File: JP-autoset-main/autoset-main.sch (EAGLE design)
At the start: 120 parts, among them J1 TERM_1X2_0.1, J10 TERM_1X2_0.1, J11 TERM_1X2_0.1, J12 TERM_1X2_0.1, J2 TERM_1X6_0.1, J3 TERM_1X2_0.1, J4 TERM_1X4_0.1, J5 TERM_1X2_0.1, J6 TERM_1X2_0.1, J7 TERM_1X2_0.1, J8 TERM_1X2_0.1, J9 TERM_1X2_0.1, P1 RECT_1X8, P2 RECT_1X6, P3 RECT_1X8, P4 RECT_1X10, Q1 NMOS-RUC002N05, Q2 NMOS-RUC002N05, Q3 NMOS-RUC002N05, Q4 NMOS-RUC002N05, Q5 NMOS-RUC002N05, Q7 PMOS-FQD7P06TM, U1 LM293DT, U10 QRE1113GR, U2 LM293DT, U3 QRE1113GR, U4 QRE1113GR, U5 QRE1113GR, U6 LD1085CDT-R, U8 A3909

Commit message: Multiple updates
Library update (add switch)
Updated sensing board to 4 layers, added some filtering.
Updated control board to 4 layers, added functionality.
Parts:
- removed D3, D4, D5, D6: LED, dsantoro-discrete:LED
- removed Z17: NC, dsantoro-dir:NC
- added R56: 0, dsantoro-discrete:R0603
- added SW1: GPTS203211B, dsantoro-sw:GPTS203211B
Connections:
- net BUTTON1: now also P3.2; no longer P3.3
- net BUTTON2: now also P3.3; no longer P3.2
- net LED1: now also P4.9; no longer P3.4
- net LED2: now also P4.8; no longer P4.7
- net LED3: now also P3.4; no longer P4.9
- net LED4: now also P4.7; no longer P4.8
- net N$12: no longer D3.C
- net N$14: no longer D3.A
- net N$16: no longer D4.A
- net N$18: no longer D5.C
- net N$19: no longer D5.A
- net N$20: no longer D6.C
- net N$23: no longer D6.A
- net N$4: no longer D4.C
- net N$5: now also R56.1, R7.2, R8.2, SW1.1; no longer P2.6, Z17.P$1
- net VCC: no longer C15.1, C16.1, C19.1, C23.1, R38.2, R39.2, R45.2, R50.2, R52.2, R53.2, R54.2, R55.2
- net VCOPT1: now also P2.1; no longer P2.4
- net VCOPT2: now also P2.2; no longer P2.3
- net VCOPT3: now also P2.3; no longer P2.2
- net VCOPT4: now also P2.4; no longer P2.1
- net VDD: now also C15.1, C16.1, C19.1, C23.1, R38.2, R39.2, R45.2, R50.2, R52.2, R53.2, R54.2, R55.2, R56.2, SW1.2; no longer R7.2, R8.2
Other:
- moved on the sheet: P1, P4, R32, R33, R7, R8

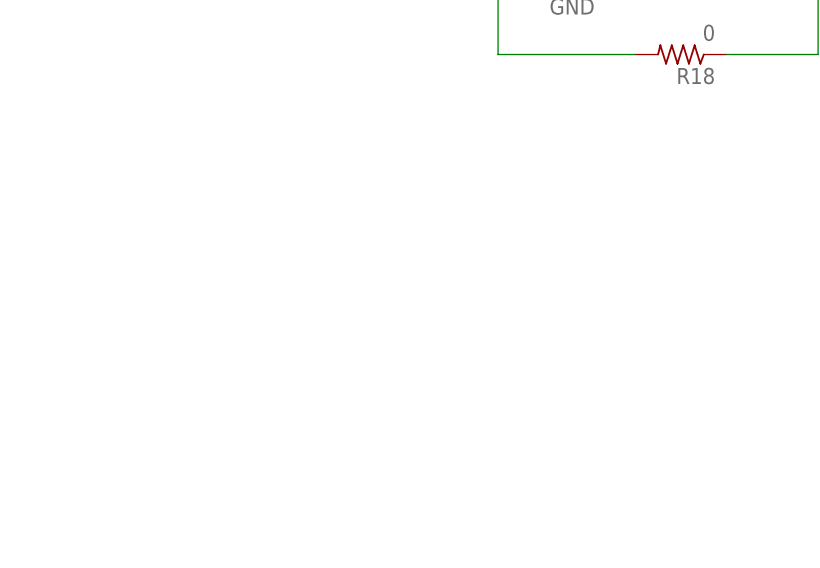
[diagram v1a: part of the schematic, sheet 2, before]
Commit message: Updates
Sensing manufacture. Updated library. Updated main schematic to include
magnetic sensor.
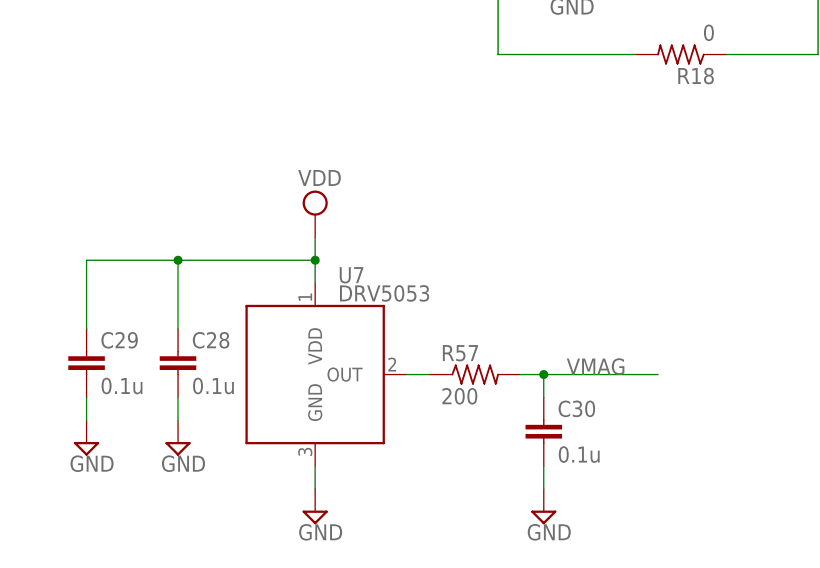
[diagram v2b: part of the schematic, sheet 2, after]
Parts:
- added C28, C29, C30: 0.1u, dsantoro-discrete:C0603
- added R57: 200, dsantoro-discrete:R0603
- added U7: DRV5053, dsantoro-sens:DRV5053
- SW1: DKPN (none) -> CW181-ND
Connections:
- new net N$25: R57.1, U7.OUT
- new net VMAG: C30.1, P2.6, R57.2
- net GND: now also C28.2, C29.2, C30.2, U7.GND
- net VDD: now also C28.1, C29.1, U7.VDD
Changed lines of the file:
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@@
 <setting verticaltext="up"/>
 </settings>
-<grid distance="0.1" unitdist="inch" unit="inch" style="lines" multiple="1" display="no" altdistance="0.025" altunitdist="inch" altunit="inch"/>
+<grid distance="0.1" unitdist="inch" unit="inch" style="lines" multiple="1" display="no" altdistance="0.01" altunitdist="inch" altunit="inch"/>
 <layers>
 <layer number="1" name="Top" color="4" fill="1" visible="no" active="no"/>
@@
 <part name="SUPPLY83" library="supply2" deviceset="VDD" device=""/>
 <part name="SUPPLY97" library="supply2" deviceset="VDD" device=""/>
-<part name="SW1" library="dsantoro-sw" deviceset="GPTS203211B" device=""/>
+<part name="SW1" library="dsantoro-sw" deviceset="GPTS203211B" device="">
+<attribute name="DKPN" value="CW181-ND"/>
+</part>
 <part name="R56" library="dsantoro-discrete" deviceset="R" device="0603" value="0">
 <attribute name="DKPN" value="541-2779-1-ND"/>
 </part>
+<part name="U7" library="dsantoro-sens" deviceset="DRV5053" device=""/>
+<part name="C28" library="dsantoro-discrete" deviceset="C" device="0603" value="0.1u">
+<attribute name="DKPN" value="490-1519-1-ND"/>
+</part>
+<part name="C29" library="dsantoro-discrete" deviceset="C" device="0603" value="0.1u">
+<attribute name="DKPN" value="490-1519-1-ND"/>
+</part>
+<part name="SUPPLY42" library="supply2" deviceset="GND" device=""/>
+<part name="SUPPLY111" library="supply2" deviceset="GND" device=""/>
+<part name="SUPPLY112" library="supply2" deviceset="VDD" device=""/>
+<part name="SUPPLY113" library="supply2" deviceset="GND" device=""/>
+<part name="R57" library="dsantoro-discrete" deviceset="R" device="0603" value="200">
+<attribute name="DKPN" value="RHM200DCT-ND"/>
+</part>
+<part name="C30" library="dsantoro-discrete" deviceset="C" device="0603" value="0.1u">
+<attribute name="DKPN" value="490-1519-1-ND"/>
+</part>
+<part name="SUPPLY114" library="supply2" deviceset="GND" device=""/>
 </parts>
 <sheets>
@@
 <instance part="SUPPLY83" gate="G$1" x="312.42" y="157.48"/>
 <instance part="SUPPLY97" gate="G$1" x="358.14" y="157.48"/>
-<instance part="SW1" gate="G$1" x="22.86" y="220.98" rot="MR0"/>
+<instance part="SW1" gate="G$1" x="22.86" y="220.98" rot="MR0">
+<attribute name="DKPN" x="22.86" y="220.98" size="1.778" layer="96" rot="MR0" display="off"/>
+</instance>
 <instance part="R56" gate="G$1" x="24.13" y="228.6" rot="R180">
 <attribute name="DKPN" x="24.13" y="228.6" size="1.778" layer="96" rot="R180" display="off"/>
@@
 <wire x1="33.02" y1="228.6" x2="33.02" y2="220.98" width="0.1524" layer="91"/>
 <junction x="33.02" y="220.98"/>
+</segment>
+</net>
+<net name="VMAG" class="0">
+<segment>
+<pinref part="P2" gate="G$1" pin="6"/>
+<wire x1="22.86" y1="139.7" x2="35.56" y2="139.7" width="0.1524" layer="91"/>
+<label x="27.94" y="139.7" size="1.778" layer="95"/>
 </segment>
 </net>
@@
 <instance part="FRAME2" gate="G$1" x="0" y="0"/>
 <instance part="FRAME2" gate="G$2" x="180.34" y="7.62"/>
+<instance part="U7" gate="G$1" x="35.56" y="35.56"/>
+<instance part="C28" gate="G$1" x="27.94" y="30.48">
+<attribute name="DKPN" x="27.94" y="30.48" size="1.778" layer="96" display="off"/>
+</instance>
+<instance part="C29" gate="G$1" x="17.78" y="30.48">
+<attribute name="DKPN" x="17.78" y="30.48" size="1.778" layer="96" display="off"/>
+</instance>
+<instance part="SUPPLY42" gate="GND" x="17.78" y="20.32"/>
+<instance part="SUPPLY111" gate="GND" x="27.94" y="20.32"/>
+<instance part="SUPPLY112" gate="G$1" x="43.18" y="45.72"/>
+<instance part="SUPPLY113" gate="GND" x="43.18" y="12.7"/>
+<instance part="R57" gate="G$1" x="60.96" y="27.94">
+<attribute name="DKPN" x="60.96" y="27.94" size="1.778" layer="96" display="off"/>
+</instance>
+<instance part="C30" gate="G$1" x="68.58" y="22.86">
+<attribute name="DKPN" x="68.58" y="22.86" size="1.778" layer="96" display="off"/>
+</instance>
+<instance part="SUPPLY114" gate="GND" x="68.58" y="12.7"/>
 </instances>
 <busses>
@@
 <pinref part="U1" gate="A" pin="V-"/>
 <pinref part="SUPPLY5" gate="GND" pin="GND"/>
+</segment>
+<segment>
+<pinref part="C29" gate="G$1" pin="2"/>
+<pinref part="SUPPLY42" gate="GND" pin="GND"/>
+<wire x1="17.78" y1="22.86" x2="17.78" y2="25.4" width="0.1524" layer="91"/>
+</segment>
+<segment>
+<pinref part="C28" gate="G$1" pin="2"/>
+<pinref part="SUPPLY111" gate="GND" pin="GND"/>
+<wire x1="27.94" y1="22.86" x2="27.94" y2="25.4" width="0.1524" layer="91"/>
+</segment>
+<segment>
+<pinref part="U7" gate="G$1" pin="GND"/>
+<pinref part="SUPPLY113" gate="GND" pin="GND"/>
+<wire x1="43.18" y1="15.24" x2="43.18" y2="17.78" width="0.1524" layer="91"/>
+</segment>
+<segment>
+<pinref part="C30" gate="G$1" pin="2"/>
+<pinref part="SUPPLY114" gate="GND" pin="GND"/>
+<wire x1="68.58" y1="15.24" x2="68.58" y2="17.78" width="0.1524" layer="91"/>
 </segment>
 </net>
@@
 <pinref part="SUPPLY3" gate="G$1" pin="VDD"/>
 </segment>
+<segment>
+<pinref part="U7" gate="G$1" pin="VDD"/>
+<pinref part="SUPPLY112" gate="G$1" pin="VDD"/>
+<wire x1="43.18" y1="43.18" x2="43.18" y2="40.64" width="0.1524" layer="91"/>
+<pinref part="C28" gate="G$1" pin="1"/>
+<wire x1="43.18" y1="40.64" x2="43.18" y2="38.1" width="0.1524" layer="91"/>
+<wire x1="43.18" y1="40.64" x2="27.94" y2="40.64" width="0.1524" layer="91"/>
+<wire x1="27.94" y1="40.64" x2="27.94" y2="33.02" width="0.1524" layer="91"/>
+<junction x="43.18" y="40.64"/>
+<pinref part="C29" gate="G$1" pin="1"/>
+<wire x1="27.94" y1="40.64" x2="17.78" y2="40.64" width="0.1524" layer="91"/>
+<wire x1="17.78" y1="40.64" x2="17.78" y2="33.02" width="0.1524" layer="91"/>
+<junction x="27.94" y="40.64"/>
+</segment>
 </net>
 <net name="N$44" class="0">
@@
 </segment>
 </net>
+<net name="N$25" class="0">
+<segment>
+<pinref part="U7" gate="G$1" pin="OUT"/>
+<pinref part="R57" gate="G$1" pin="1"/>
+<wire x1="53.34" y1="27.94" x2="55.88" y2="27.94" width="0.1524" layer="91"/>
+</segment>
+</net>
+<net name="VMAG" class="0">
+<segment>
+<pinref part="C30" gate="G$1" pin="1"/>
+<wire x1="68.58" y1="25.4" x2="68.58" y2="27.94" width="0.1524" layer="91"/>
+<pinref part="R57" gate="G$1" pin="2"/>
+<wire x1="68.58" y1="27.94" x2="66.04" y2="27.94" width="0.1524" layer="91"/>
+<wire x1="68.58" y1="27.94" x2="81.28" y2="27.94" width="0.1524" layer="91"/>
+<junction x="68.58" y="27.94"/>
+<label x="71.12" y="27.94" size="1.778" layer="95"/>
+</segment>
+</net>

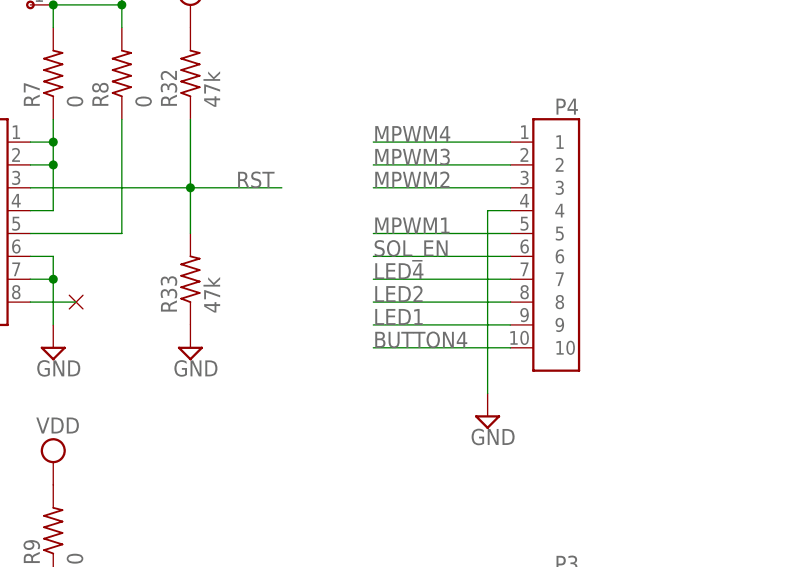
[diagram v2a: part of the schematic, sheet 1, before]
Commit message: Main Board Updates
Move things away from holes.  Create mfg files
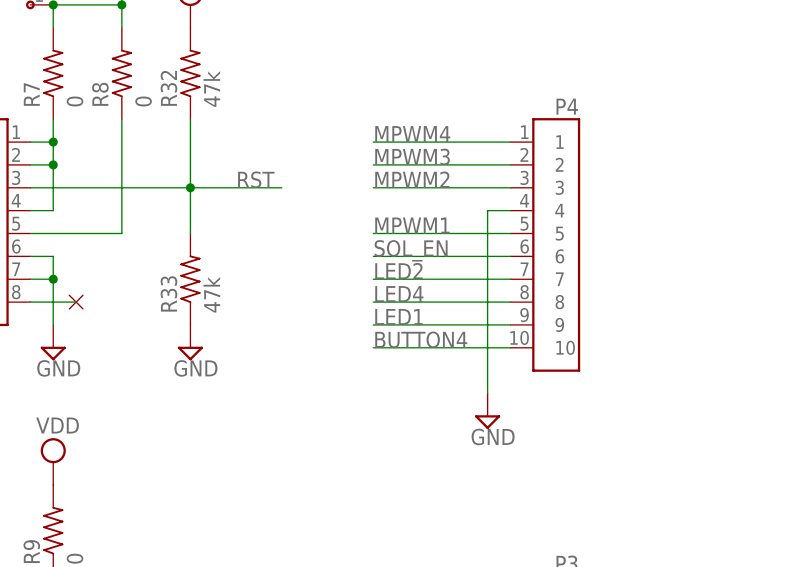
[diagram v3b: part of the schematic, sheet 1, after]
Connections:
- net LED2: now also P4.7; no longer P4.8
- net LED4: now also P4.8; no longer P4.7
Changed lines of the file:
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@@
 </segment>
 <segment>
-<pinref part="P4" gate="G$1" pin="7"/>
-<wire x1="76.2" y1="190.5" x2="60.96" y2="190.5" width="0.1524" layer="91"/>
-<label x="60.96" y="190.5" size="1.778" layer="95"/>
+<pinref part="P4" gate="G$1" pin="8"/>
+<wire x1="60.96" y1="187.96" x2="76.2" y2="187.96" width="0.1524" layer="91"/>
+<label x="60.96" y="187.96" size="1.778" layer="95"/>
 </segment>
 </net>
@@
 </segment>
 <segment>
-<pinref part="P4" gate="G$1" pin="8"/>
-<wire x1="60.96" y1="187.96" x2="76.2" y2="187.96" width="0.1524" layer="91"/>
-<label x="60.96" y="187.96" size="1.778" layer="95"/>
-</segment>
-</net>
+<pinref part="P4" gate="G$1" pin="7"/>
+<wire x1="76.2" y1="190.5" x2="60.96" y2="190.5" width="0.1524" layer="91"/>
+<label x="60.96" y="190.5" size="1.778" layer="95"/>
+</segment>
+</net>
